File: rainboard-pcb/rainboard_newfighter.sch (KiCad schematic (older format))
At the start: 98 parts, among them J1 Conn_01x02, J10 Conn_01x03, J11 SDS-50J, J12 SDS-50J, J13 Conn_01x02, J14 Conn_01x02, J15 Conn_01x02, J16 Conn_01x02, J17 Conn_01x02, J18 Conn_01x02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

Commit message: start on v0.4 of PCB
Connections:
- net softpot-1: now also XA1.A9
- net softpot-2: no longer XA1.A9
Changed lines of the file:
@@
 5V
 Text GLabel 1050 3250 0    50   Input ~ 0
-softpot-2
+softpot-1
 Wire Wire Line
 	1050 3250 1650 3250

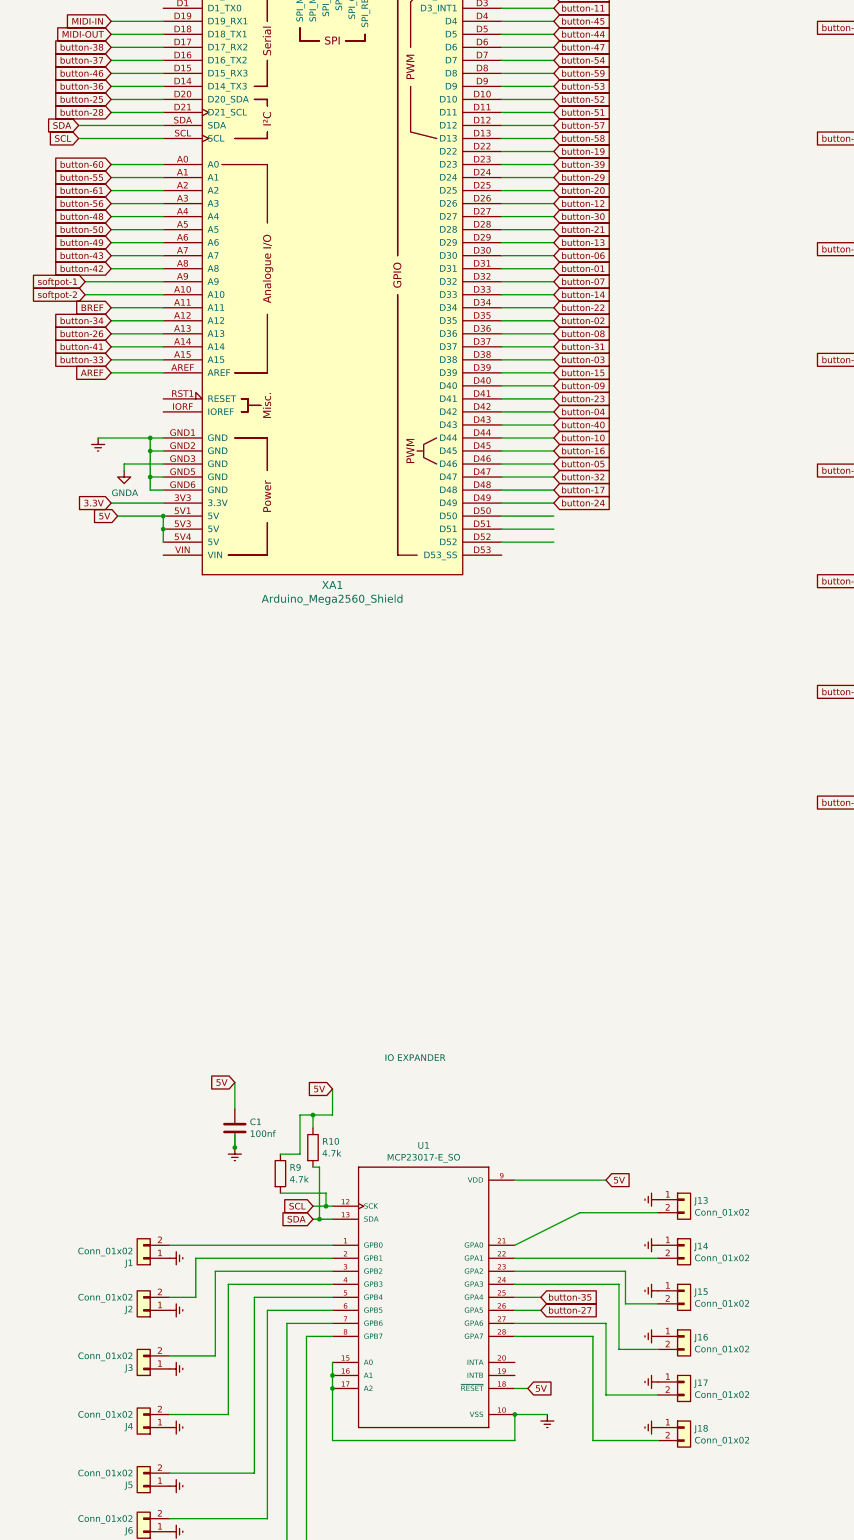
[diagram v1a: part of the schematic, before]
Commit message: fix issues with buttons 25 and 28. Improved ground and power network
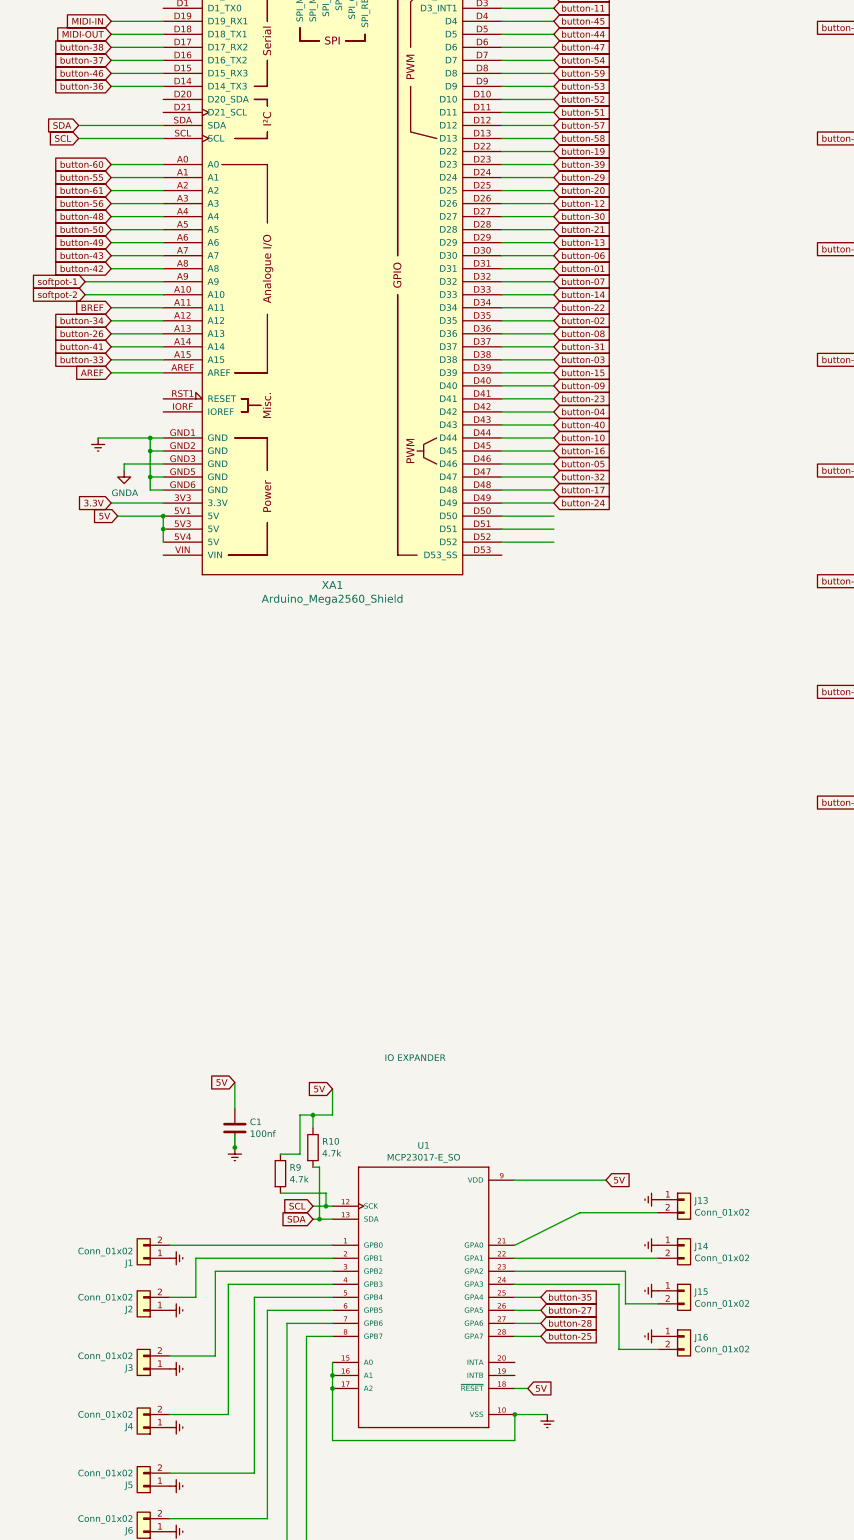
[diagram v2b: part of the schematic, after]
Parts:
- removed J17, J18: Conn_01x02, Connector_JST:JST_XH_B2B-XH-AM_1x02_P2.50mm_Vertical, symbol Connector_Generic:Conn_01x02
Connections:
- net button-25: now also U1.28 (GPA7); no longer XA1.D20 (D20_SDA)
- net button-28: now also U1.27 (GPA6); no longer XA1.D21 (D21_SCL)
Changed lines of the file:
@@
 Wire Wire Line
 	4250 5150 4650 5150
-Text GLabel 1250 1850 0    50   Input ~ 0
-button-25
 Text GLabel 4650 1150 2    50   Input ~ 0
 button-11
@@
 Wire Wire Line
 	1650 1350 1250 1350
-Text GLabel 1250 1950 0    50   Input ~ 0
-button-28
 Text GLabel 1300 5050 0    50   Input ~ 0
 5V
@@
 Wire Wire Line
 	20150 11950 20150 12050
-Wire Wire Line
-	1250 1850 1650 1850
-Wire Wire Line
-	1250 1950 1650 1950
 Text GLabel 1250 3950 0    50   Input ~ 0
 AREF
@@
 Wire Wire Line
 	4350 12150 4350 11950
-$Comp
-L Connector_Generic:Conn_01x02 J17
-U 1 1 6373D6C2
-P 5650 11700
-F 0 "J17" H 5730 11692 50  0000 L CNN
-F 1 "Conn_01x02" H 5730 11601 50  0000 L CNN
-F 2 "Connector_JST:JST_XH_B2B-XH-AM_1x02_P2.50mm_Vertical" H 5650 11700 50  0001 C CNN
-F 3 "~" H 5650 11700 50  0001 C CNN
-	1    5650 11700
-	1    0    0    -1
-$EndComp
-$Comp
-L Connector_Generic:Conn_01x02 J18
-U 1 1 6373D6C8
-P 5650 12050
-F 0 "J18" H 5730 12042 50  0000 L CNN
-F 1 "Conn_01x02" H 5730 11951 50  0000 L CNN
-F 2 "Connector_JST:JST_XH_B2B-XH-AM_1x02_P2.50mm_Vertical" H 5650 12050 50  0001 C CNN
-F 3 "~" H 5650 12050 50  0001 C CNN
-	1    5650 12050
-	1    0    0    -1
-$EndComp
-$Comp
-L power:Earth #PWR0122
-U 1 1 6373D6CE
-P 5450 11700
-F 0 "#PWR0122" H 5450 11450 50  0001 C CNN
-F 1 "Earth" H 5450 11550 50  0001 C CNN
-F 2 "" H 5450 11700 50  0001 C CNN
-F 3 "~" H 5450 11700 50  0001 C CNN
-	1    5450 11700
-	0    1    1    0
-$EndComp
-$Comp
-L power:Earth #PWR0123
-U 1 1 6373D6D4
-P 5450 12050
-F 0 "#PWR0123" H 5450 11800 50  0001 C CNN
-F 1 "Earth" H 5450 11900 50  0001 C CNN
-F 2 "" H 5450 12050 50  0001 C CNN
-F 3 "~" H 5450 12050 50  0001 C CNN
-	1    5450 12050
-	0    1    1    0
-$EndComp
-Wire Wire Line
-	5050 11800 5050 11250
-Wire Wire Line
-	5050 11250 4350 11250
-Wire Wire Line
-	5050 11800 5450 11800
-Wire Wire Line
-	4950 12150 4950 11350
-Wire Wire Line
-	4950 11350 4350 11350
-Wire Wire Line
-	4950 12150 5450 12150
 Text Notes 8650 10150 0    50   ~ 0
 SOFTPOTS
@@
 Wire Wire Line
 	14650 12200 14200 12200
+Text GLabel 4550 11350 2    50   Input ~ 0
+button-25
+Text GLabel 4550 11250 2    50   Input ~ 0
+button-28
+Wire Wire Line
+	4350 11250 4550 11250
+Wire Wire Line
+	4350 11350 4550 11350
 $EndSCHEMATC
